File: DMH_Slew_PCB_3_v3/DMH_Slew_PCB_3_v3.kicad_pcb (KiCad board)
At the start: 2 copper layers, 50 x 100 mm, 63 parts, among them J11 Conn_02x03_Top_Bottom, J12 Conn_02x06_Top_Bottom, J13 Conn_02x03_Top_Bottom, Q1 BC548, Q2 BC548, Q3 BC558, Q4 BC558, Q5 BC548, Q6 BC548, U1 TL074, U2 TL074

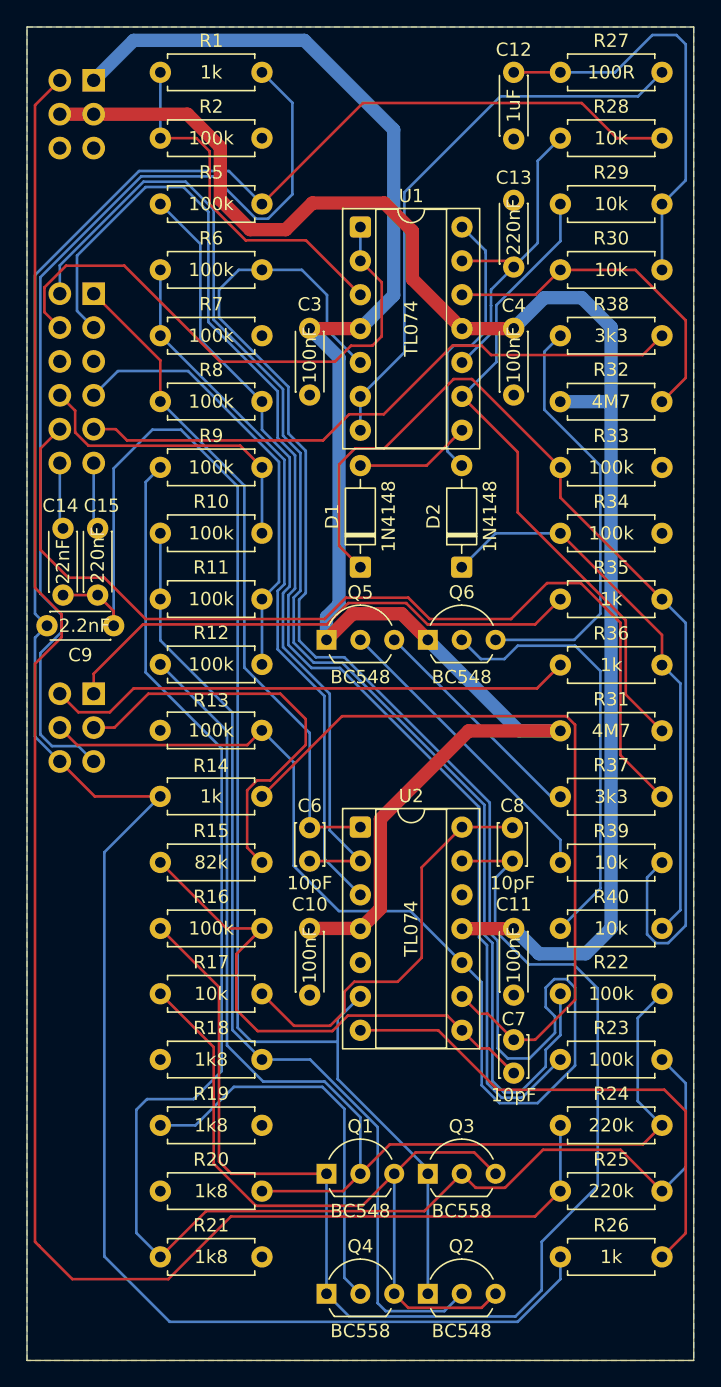
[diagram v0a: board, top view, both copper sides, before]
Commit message: Redesigned Main PCB
and regenerated Gerbers
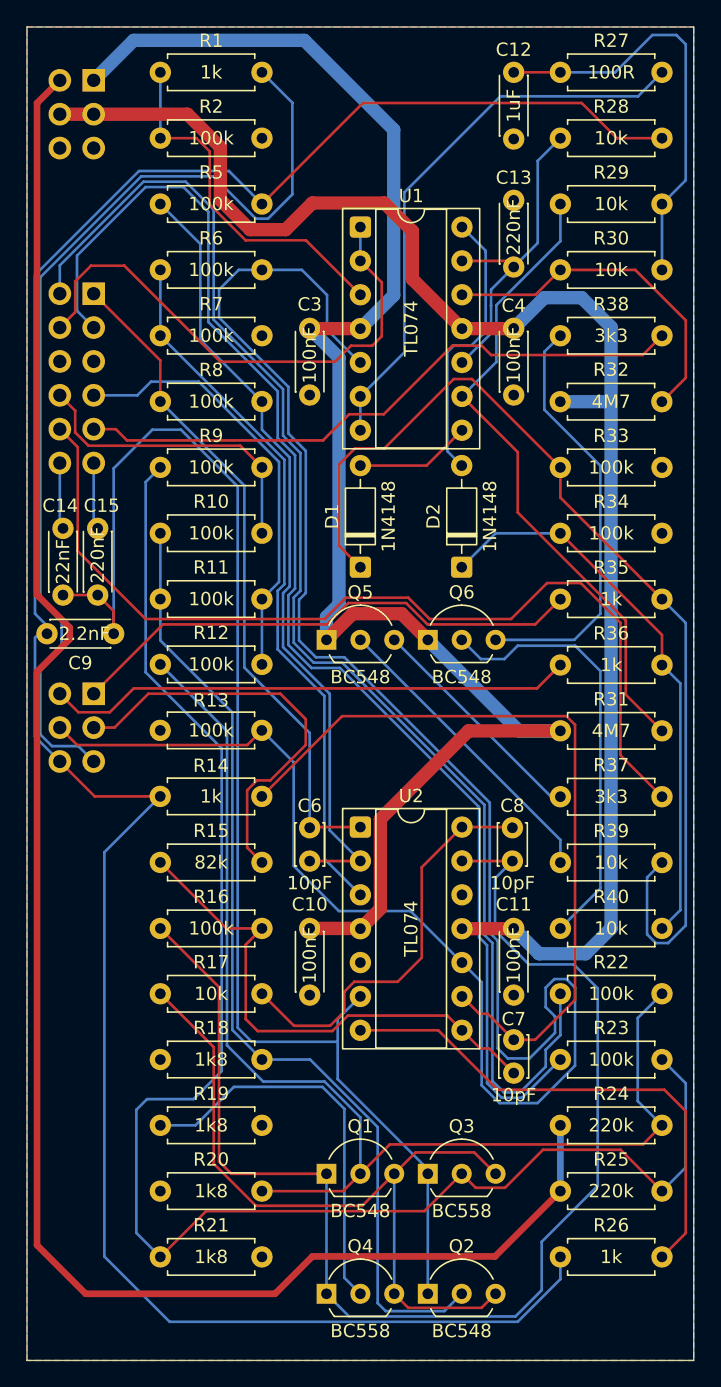
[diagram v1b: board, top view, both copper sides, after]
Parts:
- moved C9 0.60 mm to (56.5, 75.5)
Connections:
- net +10V_A renamed +10V
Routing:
- net A_F_LED_S: track 73.3 -> 70.5 mm
- net A_CV_Buff_S: track 42.1 -> 40.0 mm
- net +10V: track 137.8 -> 139.0 mm
- net A_F_Gate_Jack_S: track 40.1 -> 39.3 mm
- net A_LinLog_Sw_p5_S: track 33.2 -> 32.5 mm
- net Net-(C7-Pad2): track 40.3 -> 39.7 mm
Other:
- board text added: "Mk1.1 - April 2026"
- board text removed: "Mk1.0 - March 2026"
